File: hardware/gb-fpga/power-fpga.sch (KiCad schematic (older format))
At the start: 1 part, among them U1 xc7s25ftgb196

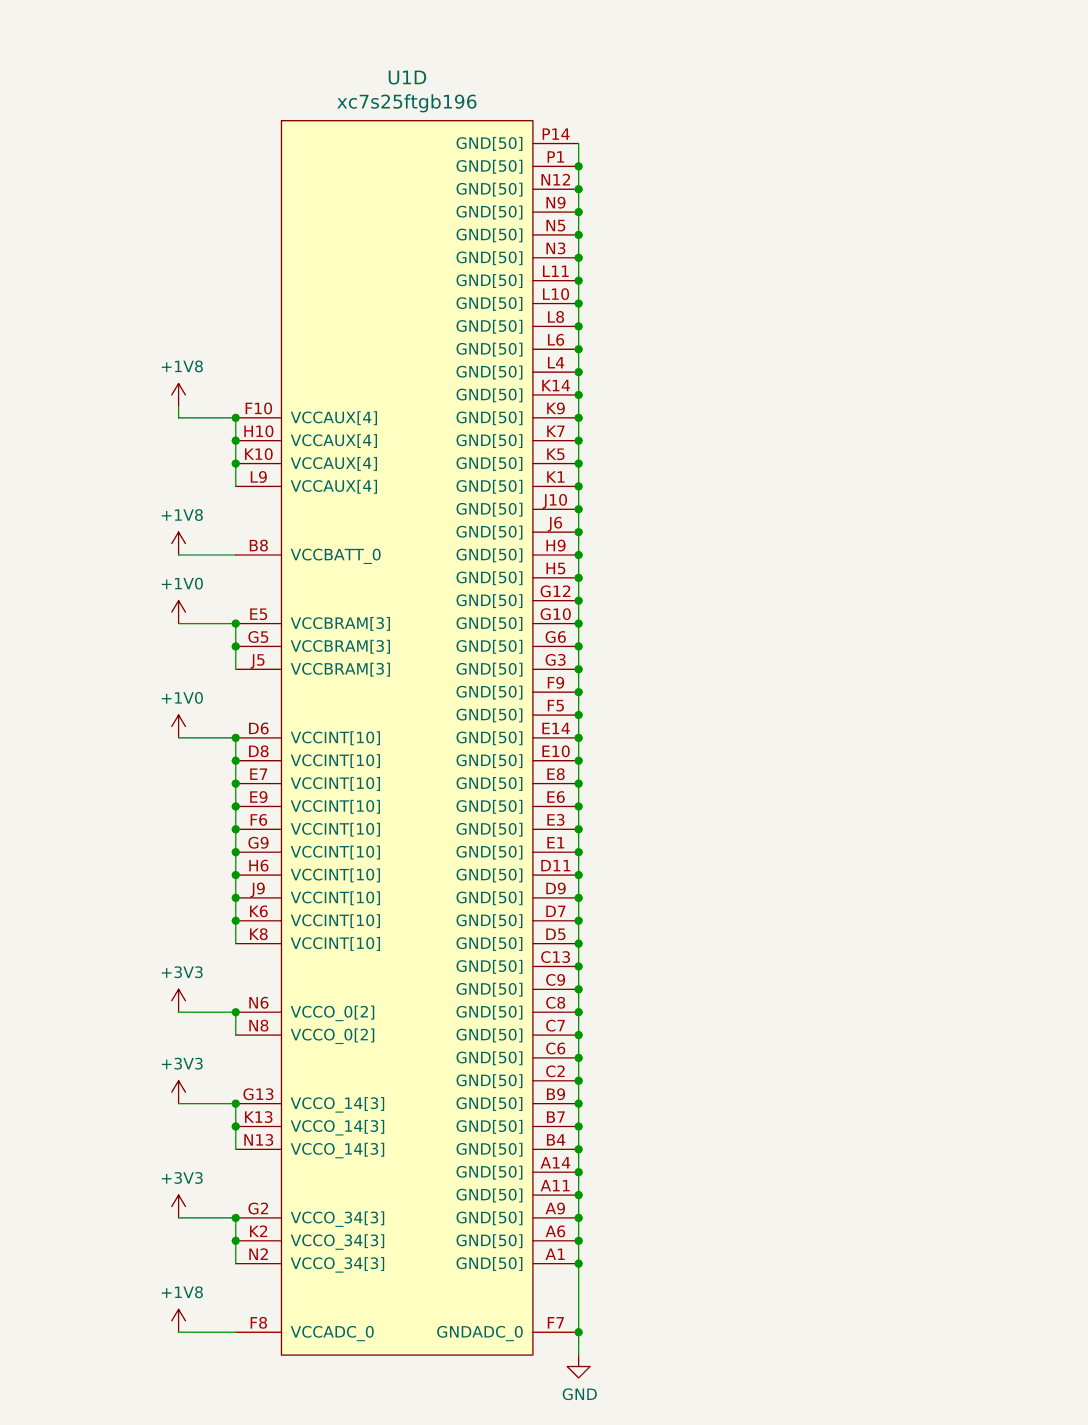
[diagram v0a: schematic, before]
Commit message: Add capacitor networks to fpga power rails
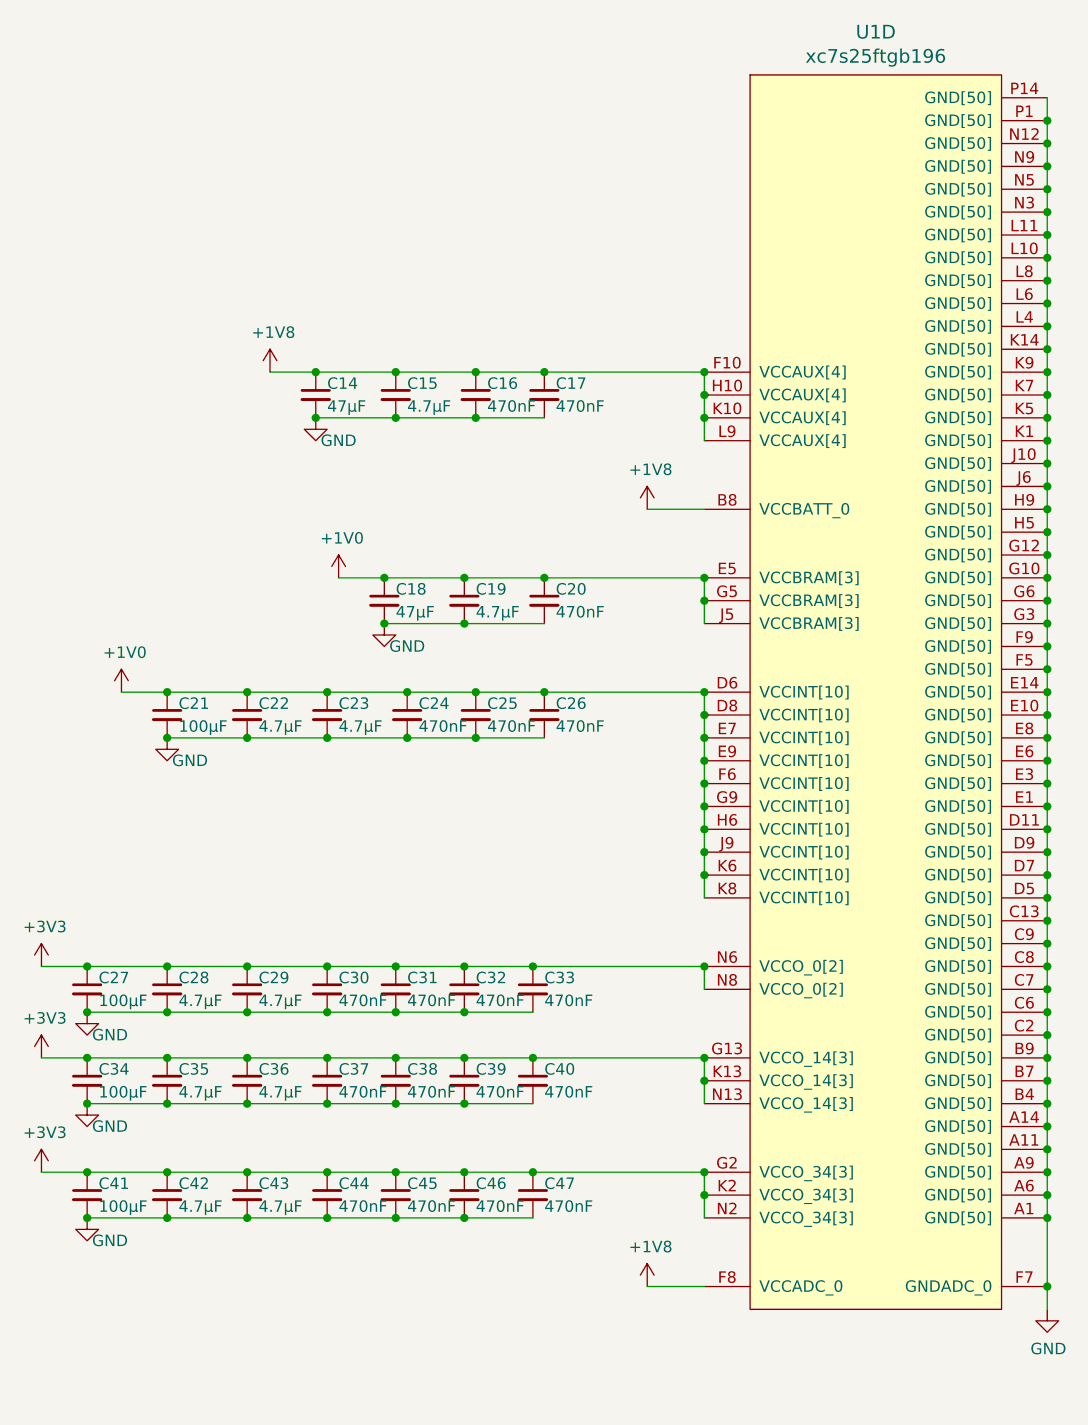
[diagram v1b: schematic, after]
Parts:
- added C14, C18: 47µF, Capacitor_SMD:C_0402_1005Metric, symbol Device:C_Small
- added C15, C19, C22, C23, C28, C29, C35, C36, C42, C43: 4.7µF, Capacitor_SMD:C_0402_1005Metric, symbol Device:C_Small
- added C16, C17, C20, C24, C25, C26, C30, C31, C32, C33, C37, C38, C39, C40, C44, C45, C46, C47: 470nF, Capacitor_SMD:C_0402_1005Metric, symbol Device:C_Small
- added C21, C27, C34, C41: 100µF, Capacitor_SMD:C_0402_1005Metric, symbol Device:C_Small
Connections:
- net +1V0: now also C18.1, C19.1, C20.1, C21.1, C22.1, C23.1, C24.1, C25.1, C26.1
- net +1V8: now also C14.1, C15.1, C16.1, C17.1
- net +3V3: now also C27.1, C28.1, C29.1, C30.1, C31.1, C32.1, C33.1, C34.1, C35.1, C36.1, C37.1, C38.1, C39.1, C40.1, C41.1, C42.1, C43.1, C44.1, C45.1, C46.1, C47.1
- net GND: now also C14.2, C15.2, C16.2, C17.2, C18.2, C19.2, C20.2, C21.2, C22.2, C23.2, C24.2, C25.2, C26.2, C27.2, C28.2, C29.2, C30.2, C31.2, C32.2, C33.2, C34.2, C35.2, C36.2, C37.2, C38.2, C39.2, C40.2, C41.2, C42.2, C43.2, C44.2, C45.2, C46.2, C47.2
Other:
- moved on the sheet: U1D

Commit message: Switch to 0201 footprints for fpga power caps
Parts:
- C14, C15, C16, C17, C18, C19, C20, C21, C22, C23, C24, C25, C26, C27, C28, C29, C30, C31, C32, C33, C34, C35, C36, C37, C38, C39, C40, C41, C42, C43, C44, C45, C46, C47: footprint Capacitor_SMD:C_0402_1005Metric -> Capacitor_SMD:C_0201_0603Metric
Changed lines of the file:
@@
 F 0 "C44" H 3550 5850 50  0000 L CNN
 F 1 "470nF" H 3550 5750 50  0000 L CNN
-F 2 "Capacitor_SMD:C_0402_1005Metric" H 3500 5800 50  0001 C CNN
+F 2 "Capacitor_SMD:C_0201_0603Metric" H 3500 5800 50  0001 C CNN
 F 3 "~" H 3500 5800 50  0001 C CNN
 	1    3500 5800
@@
 F 0 "C43" H 3200 5850 50  0000 L CNN
 F 1 "4.7µF" H 3200 5750 50  0000 L CNN
-F 2 "Capacitor_SMD:C_0402_1005Metric" H 3150 5800 50  0001 C CNN
+F 2 "Capacitor_SMD:C_0201_0603Metric" H 3150 5800 50  0001 C CNN
 F 3 "~" H 3150 5800 50  0001 C CNN
 	1    3150 5800
@@
 F 0 "C45" H 3850 5850 50  0000 L CNN
 F 1 "470nF" H 3850 5750 50  0000 L CNN
-F 2 "Capacitor_SMD:C_0402_1005Metric" H 3800 5800 50  0001 C CNN
+F 2 "Capacitor_SMD:C_0201_0603Metric" H 3800 5800 50  0001 C CNN
 F 3 "~" H 3800 5800 50  0001 C CNN
 	1    3800 5800
@@
 F 0 "C46" H 4150 5850 50  0000 L CNN
 F 1 "470nF" H 4150 5750 50  0000 L CNN
-F 2 "Capacitor_SMD:C_0402_1005Metric" H 4100 5800 50  0001 C CNN
+F 2 "Capacitor_SMD:C_0201_0603Metric" H 4100 5800 50  0001 C CNN
 F 3 "~" H 4100 5800 50  0001 C CNN
 	1    4100 5800
@@
 F 0 "C47" H 4450 5850 50  0000 L CNN
 F 1 "470nF" H 4450 5750 50  0000 L CNN
-F 2 "Capacitor_SMD:C_0402_1005Metric" H 4400 5800 50  0001 C CNN
+F 2 "Capacitor_SMD:C_0201_0603Metric" H 4400 5800 50  0001 C CNN
 F 3 "~" H 4400 5800 50  0001 C CNN
 	1    4400 5800
@@
 F 0 "C42" H 2850 5850 50  0000 L CNN
 F 1 "4.7µF" H 2850 5750 50  0000 L CNN
-F 2 "Capacitor_SMD:C_0402_1005Metric" H 2800 5800 50  0001 C CNN
+F 2 "Capacitor_SMD:C_0201_0603Metric" H 2800 5800 50  0001 C CNN
 F 3 "~" H 2800 5800 50  0001 C CNN
 	1    2800 5800
@@
 F 0 "C41" H 2500 5850 50  0000 L CNN
 F 1 "100µF" H 2500 5750 50  0000 L CNN
-F 2 "Capacitor_SMD:C_0402_1005Metric" H 2450 5800 50  0001 C CNN
+F 2 "Capacitor_SMD:C_0201_0603Metric" H 2450 5800 50  0001 C CNN
 F 3 "~" H 2450 5800 50  0001 C CNN
 	1    2450 5800
@@
 F 0 "C37" H 3550 5350 50  0000 L CNN
 F 1 "470nF" H 3550 5250 50  0000 L CNN
-F 2 "Capacitor_SMD:C_0402_1005Metric" H 3500 5300 50  0001 C CNN
+F 2 "Capacitor_SMD:C_0201_0603Metric" H 3500 5300 50  0001 C CNN
 F 3 "~" H 3500 5300 50  0001 C CNN
 	1    3500 5300
@@
 F 0 "C36" H 3200 5350 50  0000 L CNN
 F 1 "4.7µF" H 3200 5250 50  0000 L CNN
-F 2 "Capacitor_SMD:C_0402_1005Metric" H 3150 5300 50  0001 C CNN
+F 2 "Capacitor_SMD:C_0201_0603Metric" H 3150 5300 50  0001 C CNN
 F 3 "~" H 3150 5300 50  0001 C CNN
 	1    3150 5300
@@
 F 0 "C38" H 3850 5350 50  0000 L CNN
 F 1 "470nF" H 3850 5250 50  0000 L CNN
-F 2 "Capacitor_SMD:C_0402_1005Metric" H 3800 5300 50  0001 C CNN
+F 2 "Capacitor_SMD:C_0201_0603Metric" H 3800 5300 50  0001 C CNN
 F 3 "~" H 3800 5300 50  0001 C CNN
 	1    3800 5300
@@
 F 0 "C39" H 4150 5350 50  0000 L CNN
 F 1 "470nF" H 4150 5250 50  0000 L CNN
-F 2 "Capacitor_SMD:C_0402_1005Metric" H 4100 5300 50  0001 C CNN
+F 2 "Capacitor_SMD:C_0201_0603Metric" H 4100 5300 50  0001 C CNN
 F 3 "~" H 4100 5300 50  0001 C CNN
 	1    4100 5300
@@
 F 0 "C40" H 4450 5350 50  0000 L CNN
 F 1 "470nF" H 4450 5250 50  0000 L CNN
-F 2 "Capacitor_SMD:C_0402_1005Metric" H 4400 5300 50  0001 C CNN
+F 2 "Capacitor_SMD:C_0201_0603Metric" H 4400 5300 50  0001 C CNN
 F 3 "~" H 4400 5300 50  0001 C CNN
 	1    4400 5300
@@
 F 0 "C35" H 2850 5350 50  0000 L CNN
 F 1 "4.7µF" H 2850 5250 50  0000 L CNN
-F 2 "Capacitor_SMD:C_0402_1005Metric" H 2800 5300 50  0001 C CNN
+F 2 "Capacitor_SMD:C_0201_0603Metric" H 2800 5300 50  0001 C CNN
 F 3 "~" H 2800 5300 50  0001 C CNN
 	1    2800 5300
@@
 F 0 "C34" H 2500 5350 50  0000 L CNN
 F 1 "100µF" H 2500 5250 50  0000 L CNN
-F 2 "Capacitor_SMD:C_0402_1005Metric" H 2450 5300 50  0001 C CNN
+F 2 "Capacitor_SMD:C_0201_0603Metric" H 2450 5300 50  0001 C CNN
 F 3 "~" H 2450 5300 50  0001 C CNN
 	1    2450 5300
@@
 F 0 "C27" H 2500 4950 50  0000 L CNN
 F 1 "100µF" H 2500 4850 50  0000 L CNN
-F 2 "Capacitor_SMD:C_0402_1005Metric" H 2450 4900 50  0001 C CNN
+F 2 "Capacitor_SMD:C_0201_0603Metric" H 2450 4900 50  0001 C CNN
 F 3 "~" H 2450 4900 50  0001 C CNN
 	1    2450 4900
@@
 F 0 "C28" H 2850 4950 50  0000 L CNN
 F 1 "4.7µF" H 2850 4850 50  0000 L CNN
-F 2 "Capacitor_SMD:C_0402_1005Metric" H 2800 4900 50  0001 C CNN
+F 2 "Capacitor_SMD:C_0201_0603Metric" H 2800 4900 50  0001 C CNN
 F 3 "~" H 2800 4900 50  0001 C CNN
 	1    2800 4900
@@
 F 0 "C33" H 4450 4950 50  0000 L CNN
 F 1 "470nF" H 4450 4850 50  0000 L CNN
-F 2 "Capacitor_SMD:C_0402_1005Metric" H 4400 4900 50  0001 C CNN
+F 2 "Capacitor_SMD:C_0201_0603Metric" H 4400 4900 50  0001 C CNN
 F 3 "~" H 4400 4900 50  0001 C CNN
 	1    4400 4900
@@
 F 0 "C32" H 4150 4950 50  0000 L CNN
 F 1 "470nF" H 4150 4850 50  0000 L CNN
-F 2 "Capacitor_SMD:C_0402_1005Metric" H 4100 4900 50  0001 C CNN
+F 2 "Capacitor_SMD:C_0201_0603Metric" H 4100 4900 50  0001 C CNN
 F 3 "~" H 4100 4900 50  0001 C CNN
 	1    4100 4900
@@
 F 0 "C31" H 3850 4950 50  0000 L CNN
 F 1 "470nF" H 3850 4850 50  0000 L CNN
-F 2 "Capacitor_SMD:C_0402_1005Metric" H 3800 4900 50  0001 C CNN
+F 2 "Capacitor_SMD:C_0201_0603Metric" H 3800 4900 50  0001 C CNN
 F 3 "~" H 3800 4900 50  0001 C CNN
 	1    3800 4900
@@
 F 0 "C29" H 3200 4950 50  0000 L CNN
 F 1 "4.7µF" H 3200 4850 50  0000 L CNN
-F 2 "Capacitor_SMD:C_0402_1005Metric" H 3150 4900 50  0001 C CNN
+F 2 "Capacitor_SMD:C_0201_0603Metric" H 3150 4900 50  0001 C CNN
 F 3 "~" H 3150 4900 50  0001 C CNN
 	1    3150 4900
@@
 F 0 "C30" H 3550 4950 50  0000 L CNN
 F 1 "470nF" H 3550 4850 50  0000 L CNN
-F 2 "Capacitor_SMD:C_0402_1005Metric" H 3500 4900 50  0001 C CNN
+F 2 "Capacitor_SMD:C_0201_0603Metric" H 3500 4900 50  0001 C CNN
 F 3 "~" H 3500 4900 50  0001 C CNN
 	1    3500 4900
@@
 F 0 "C24" H 3900 3750 50  0000 L CNN
 F 1 "470nF" H 3900 3650 50  0000 L CNN
-F 2 "Capacitor_SMD:C_0402_1005Metric" H 3850 3700 50  0001 C CNN
+F 2 "Capacitor_SMD:C_0201_0603Metric" H 3850 3700 50  0001 C CNN
 F 3 "~" H 3850 3700 50  0001 C CNN
 	1    3850 3700
@@
 F 0 "C23" H 3550 3750 50  0000 L CNN
 F 1 "4.7µF" H 3550 3650 50  0000 L CNN
-F 2 "Capacitor_SMD:C_0402_1005Metric" H 3500 3700 50  0001 C CNN
+F 2 "Capacitor_SMD:C_0201_0603Metric" H 3500 3700 50  0001 C CNN
 F 3 "~" H 3500 3700 50  0001 C CNN
 	1    3500 3700
@@
 F 0 "C25" H 4200 3750 50  0000 L CNN
 F 1 "470nF" H 4200 3650 50  0000 L CNN
-F 2 "Capacitor_SMD:C_0402_1005Metric" H 4150 3700 50  0001 C CNN
+F 2 "Capacitor_SMD:C_0201_0603Metric" H 4150 3700 50  0001 C CNN
 F 3 "~" H 4150 3700 50  0001 C CNN
 	1    4150 3700
@@
 F 0 "C26" H 4500 3750 50  0000 L CNN
 F 1 "470nF" H 4500 3650 50  0000 L CNN
-F 2 "Capacitor_SMD:C_0402_1005Metric" H 4450 3700 50  0001 C CNN
+F 2 "Capacitor_SMD:C_0201_0603Metric" H 4450 3700 50  0001 C CNN
 F 3 "~" H 4450 3700 50  0001 C CNN
 	1    4450 3700
@@
 F 0 "C22" H 3200 3750 50  0000 L CNN
 F 1 "4.7µF" H 3200 3650 50  0000 L CNN
-F 2 "Capacitor_SMD:C_0402_1005Metric" H 3150 3700 50  0001 C CNN
+F 2 "Capacitor_SMD:C_0201_0603Metric" H 3150 3700 50  0001 C CNN
 F 3 "~" H 3150 3700 50  0001 C CNN
 	1    3150 3700
@@
 F 0 "C21" H 2850 3750 50  0000 L CNN
 F 1 "100µF" H 2850 3650 50  0000 L CNN
-F 2 "Capacitor_SMD:C_0402_1005Metric" H 2800 3700 50  0001 C CNN
+F 2 "Capacitor_SMD:C_0201_0603Metric" H 2800 3700 50  0001 C CNN
 F 3 "~" H 2800 3700 50  0001 C CNN
 	1    2800 3700
@@
 F 0 "C20" H 4500 3250 50  0000 L CNN
 F 1 "470nF" H 4500 3150 50  0000 L CNN
-F 2 "Capacitor_SMD:C_0402_1005Metric" H 4450 3200 50  0001 C CNN
+F 2 "Capacitor_SMD:C_0201_0603Metric" H 4450 3200 50  0001 C CNN
 F 3 "~" H 4450 3200 50  0001 C CNN
 	1    4450 3200
@@
 F 0 "C19" H 4150 3250 50  0000 L CNN
 F 1 "4.7µF" H 4150 3150 50  0000 L CNN
-F 2 "Capacitor_SMD:C_0402_1005Metric" H 4100 3200 50  0001 C CNN
+F 2 "Capacitor_SMD:C_0201_0603Metric" H 4100 3200 50  0001 C CNN
 F 3 "~" H 4100 3200 50  0001 C CNN
 	1    4100 3200
@@
 F 0 "C18" H 3800 3250 50  0000 L CNN
 F 1 "47µF" H 3800 3150 50  0000 L CNN
-F 2 "Capacitor_SMD:C_0402_1005Metric" H 3750 3200 50  0001 C CNN
+F 2 "Capacitor_SMD:C_0201_0603Metric" H 3750 3200 50  0001 C CNN
 F 3 "~" H 3750 3200 50  0001 C CNN
 	1    3750 3200
@@
 F 0 "C16" H 4200 2350 50  0000 L CNN
 F 1 "470nF" H 4200 2250 50  0000 L CNN
-F 2 "Capacitor_SMD:C_0402_1005Metric" H 4150 2300 50  0001 C CNN
+F 2 "Capacitor_SMD:C_0201_0603Metric" H 4150 2300 50  0001 C CNN
 F 3 "~" H 4150 2300 50  0001 C CNN
 	1    4150 2300
@@
 F 0 "C15" H 3850 2350 50  0000 L CNN
 F 1 "4.7µF" H 3850 2250 50  0000 L CNN
-F 2 "Capacitor_SMD:C_0402_1005Metric" H 3800 2300 50  0001 C CNN
+F 2 "Capacitor_SMD:C_0201_0603Metric" H 3800 2300 50  0001 C CNN
 F 3 "~" H 3800 2300 50  0001 C CNN
 	1    3800 2300
@@
 F 0 "C14" H 3500 2350 50  0000 L CNN
 F 1 "47µF" H 3500 2250 50  0000 L CNN
-F 2 "Capacitor_SMD:C_0402_1005Metric" H 3450 2300 50  0001 C CNN
+F 2 "Capacitor_SMD:C_0201_0603Metric" H 3450 2300 50  0001 C CNN
 F 3 "~" H 3450 2300 50  0001 C CNN
 	1    3450 2300
@@
 F 0 "C17" H 4500 2350 50  0000 L CNN
 F 1 "470nF" H 4500 2250 50  0000 L CNN
-F 2 "Capacitor_SMD:C_0402_1005Metric" H 4450 2300 50  0001 C CNN
+F 2 "Capacitor_SMD:C_0201_0603Metric" H 4450 2300 50  0001 C CNN
 F 3 "~" H 4450 2300 50  0001 C CNN
 	1    4450 2300
